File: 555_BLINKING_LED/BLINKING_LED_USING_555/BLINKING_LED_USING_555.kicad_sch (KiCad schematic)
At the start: 14 parts, among them U1 ICM7555xB, U2 ICM7555xB

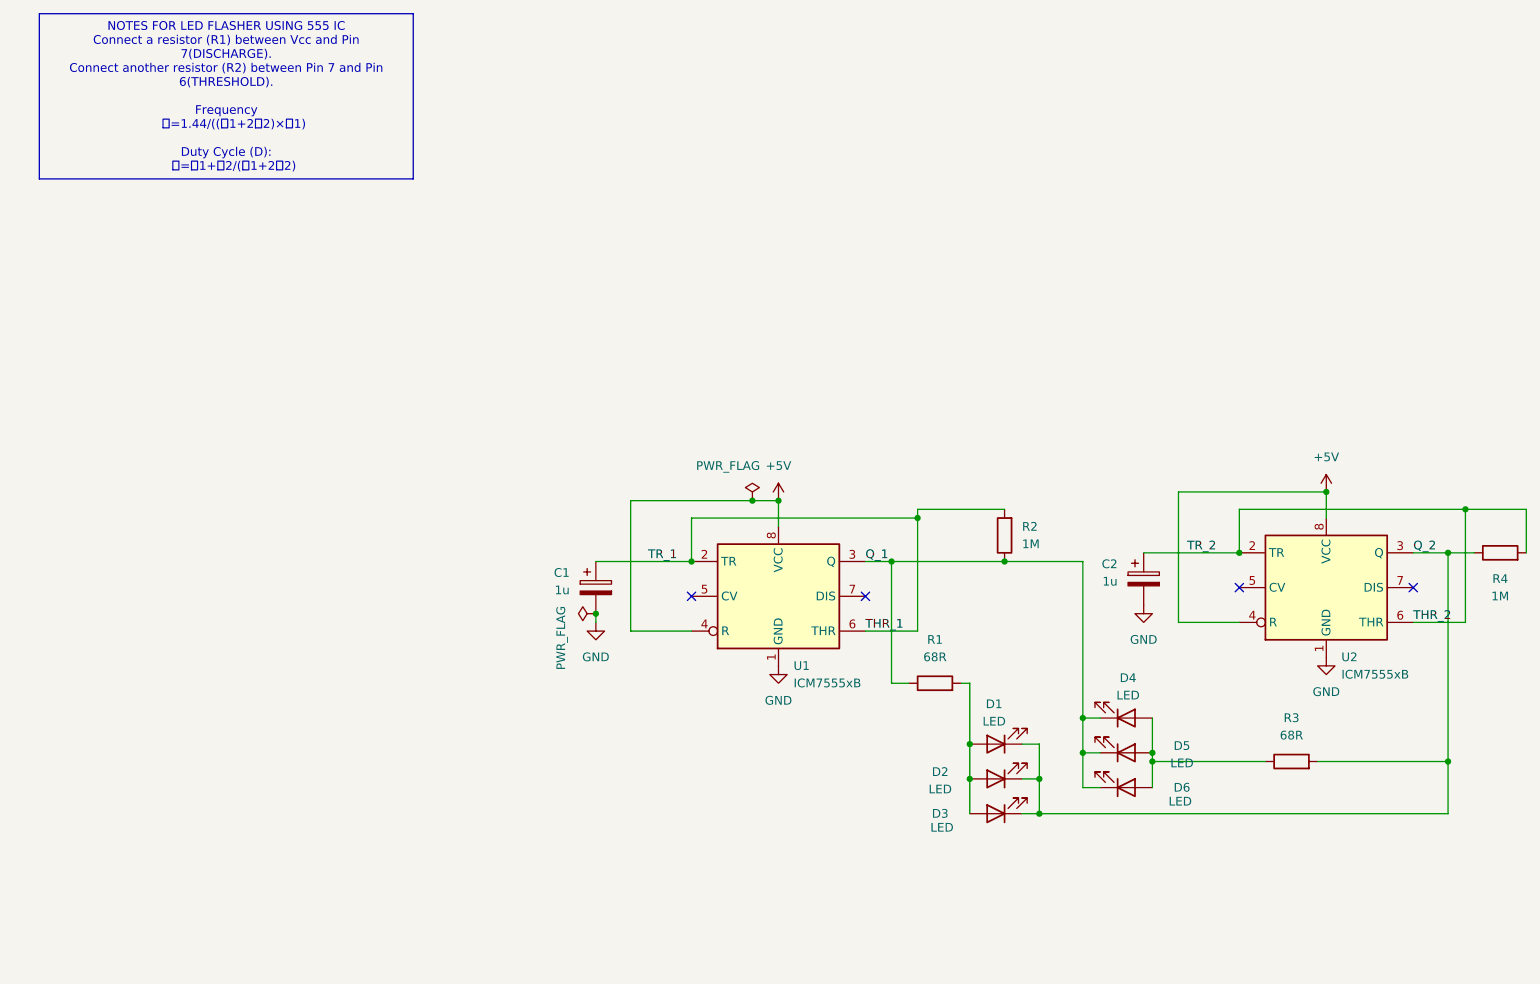
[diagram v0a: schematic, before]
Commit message: temp sensor module refined and audio amplifier made
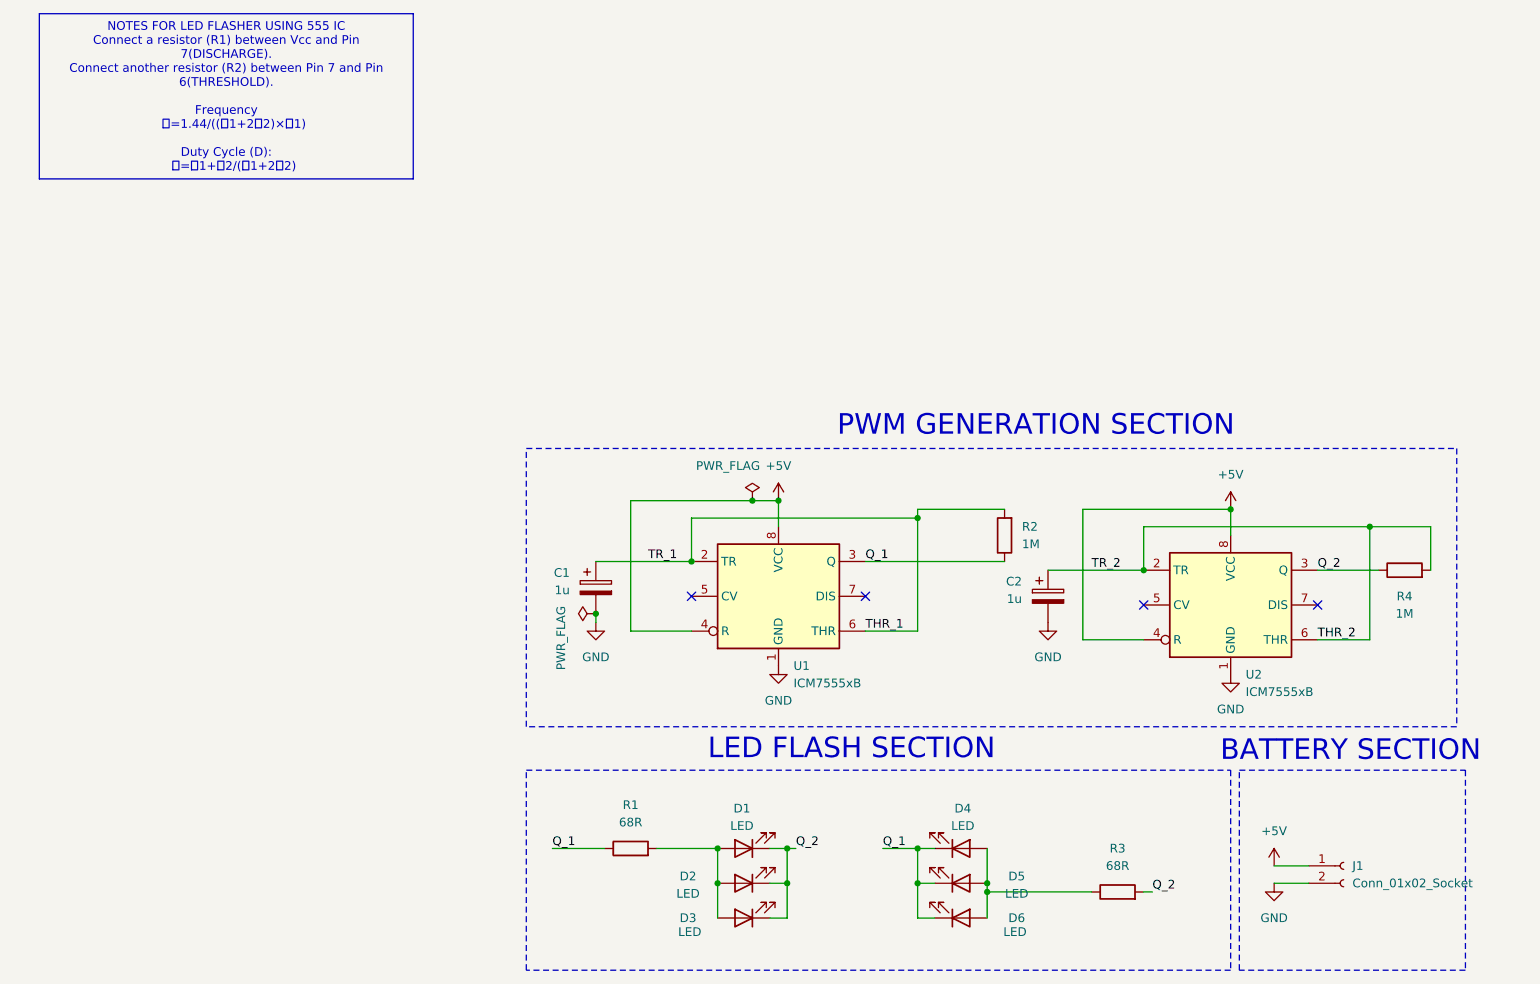
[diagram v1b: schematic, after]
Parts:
- added J1: Conn_01x02_Socket, Connector_PinHeader_2.54mm:PinHeader_1x02_P2.54mm_Vertical, symbol Connector:Conn_01x02_Socket
- U1: footprint Package_SO:SOIC-8-N7_3.9x4.9mm_P1.27mm -> Package_SO:SOIC-8_3.9x4.9mm_P1.27mm
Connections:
- net +5V: now also J1.1 (Pin_1)
- net GND: now also J1.2 (Pin_2)
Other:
- note added: "BATTERY SECTION"
- note added: "LED FLASH SECTION"
- note added: "PWM GENERATION SECTION"
- moved on the sheet: C2, D1, D2, D3, D4, D5, D6, R1, R3, R4, U2
